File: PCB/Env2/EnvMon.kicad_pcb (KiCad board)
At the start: 2 copper layers, 70 x 70 mm, 37 parts, among them J1 LCD, J2 DC, J3 TEMP, J4 LCD, J5 Reset, J6 USB-C-Socket-H, J7 TC2030-USB-NL-DS, J8 T6793, U1 ESP32-S3-MINI-1, U2 SCD41, U3 MD8942, U7 SHT40, U8 VEML6040

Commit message: Tracked and SS
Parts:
- removed C5: 100nF, RevK:C_0402
- removed U7: SHT40, RevK:Sensirion_DFN-4_1.5x1.5mm_P0.5mm_SHT4x
- added C6: 100nF, RevK:C_0402, F.Cu at (107.8, 81.8)
- added R6: 10K, RevK:R_0402, F.Cu at (98.8, 92.0)
- added R7: 10K, RevK:R_0402, F.Cu at (98.8, 89.8)
- added U4: MCP9808_MSOP, Package_SO:MSOP-8_3x3mm_P0.65mm, F.Cu at (113.0, 78.2)
- J4: footprint RevK:PinSocket_1x08_P2.54mm_Vertical_SMD -> RevK:PinHeader_1x08_P2.54mm_Vertical; moved to B.Cu
- moved D19 7.50 mm to (90.0, 98.5)
- moved R3 5.85 mm to (114.5, 106.5)
- moved R4 4.00 mm to (114.5, 105.0)
- moved D20 2.61 mm to (102.8, 103.5), turned to 90 degrees
- moved C4 1.89 mm to (99.7, 97.1), turned to 90 degrees
- moved R13 1.52 mm to (121.0, 111.8), turned to 180 degrees
- moved C3 1.00 mm to (99.5, 82.0)
- moved R5 1.00 mm to (99.5, 83.0), turned to 180 degrees
- moved C1 0.50 mm to (80.5, 82.5), turned to 180 degrees
- moved C2 0.50 mm to (80.5, 83.5), turned to 180 degrees
- moved J4 0.50 mm to (126.5, 83.4), turned to 180 degrees
- moved J6 0.50 mm to (108.8, 104.0)
- moved U8 0.50 mm to (77.0, 76.5)
- moved J3 0.25 mm to (121.8, 119.0)
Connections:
- C4 pad 1: +3V3 -> +3.3V
- D19 pad 1: DC -> VDC
- D20 pad 1: DC -> VDC
- U1 pad 10: unconnected-(U1-GPIO6-Pad10) -> CS
- U1 pad 11: unconnected-(U1-GPIO7-Pad11) -> DC
- U1 pad 12: unconnected-(U1-GPIO8-Pad12) -> RST
- U1 pad 13: unconnected-(U1-GPIO9-Pad13) -> BL
- U1 pad 18: +3.3V -> unconnected-(U1-GPIO14-Pad18)
- U1 pad 32: unconnected-(U1-GPIO36-Pad32) -> LED
- U1 pad 41: LED -> unconnected-(U1-GPIO45-Pad41)
- U1 pad 8: unconnected-(U1-GPIO4-Pad8) -> DIN
- U1 pad 9: unconnected-(U1-GPIO5-Pad9) -> CLK
- U3 pad 5: DC -> VDC
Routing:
- net +3.3V: track 0.00 -> 230.6 mm, vias 0 -> 7
- net SDA: track 0.00 -> 132.3 mm, vias 0 -> 5
- net SCL: track 0.00 -> 126.5 mm, vias 0 -> 4
- net BL: track 0.00 -> 72.5 mm
- net TEMP: track 0.00 -> 70.4 mm, vias 0 -> 4
- net RST: track 0.00 -> 69.1 mm
- net DC: track 0.00 -> 67.2 mm
- net CLK: track 0.00 -> 64.8 mm
- net DIN: track 0.00 -> 64.4 mm
- net CS: track 0.00 -> 63.2 mm
- net D+: track 0.00 -> 42.7 mm, vias 0 -> 2
- net LED: track 0.00 -> 41.3 mm, vias 0 -> 2
- net D-: track 0.00 -> 36.1 mm, vias 0 -> 2
- net VDC: track 0.00 -> 22.5 mm, vias 0 -> 2
- net GND: track 0.00 -> 21.6 mm, vias 38 -> 98
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- added copper zone on F.Cu, net VBUS
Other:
- board text added: "${CURRENT_DATE}"
- board text added: "+"
- board text added: "12"
- board text added: "2.4{dblquote}LCD"
- board text added: "21"
- board text added: "2{dblquote}LCD"
- board text added: "36"
- board text added: "39 40"
- board text added: "4 5 6 7 8 9"
- board text added: "A"
- board text added: "AB"
- board text added: "DC"
- board text added: "DIN CLK CS DC RST BL"
- board text added: "DS18B20"
- board text added: "Environmental Monitor"
- board text added: "MCP9808"
- board text added: "SCD41"
- board text added: "SDA SCL"
- board text added: "T+H"
- board text added: "T6793 or"
- board text added: "TC2030"
- board text added: "VEML6040"

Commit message: Tracking
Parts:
- moved J5 0.21 mm to (90.0, 88.0)
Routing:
- net +3.3V: track 230.6 -> 231.6 mm
- added copper zone on F.Cu, net +3.3V
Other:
- board text added: "CO2 SENSOR"
- board text added: "Made in China for Andrews&Arnold Ltd"

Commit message: Render
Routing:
- net +3.3V: track 231.6 -> 231.0 mm

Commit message: Tweaks and render
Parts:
- added J10: Conn_01x01, RevK:PinHeader_1x01_P2.54mm_Vertical, F.Cu at (101.2, 120.8)
- added J11: Conn_01x01, RevK:PinHeader_1x01_P2.54mm_Vertical, F.Cu at (101.2, 123.8)
- added J12: Conn_01x01, RevK:PinHeader_1x01_P2.54mm_Vertical, F.Cu at (101.2, 114.5)
- added J9: Conn_01x01, RevK:PinHeader_1x01_P2.54mm_Vertical, F.Cu at (101.2, 111.5)
- J8: footprint Connector_PinSocket_2.54mm:PinSocket_1x06_P2.54mm_Vertical -> RevK:PinHeader_1x06_P2.54mm_Vertical
- moved J8 0.25 mm to (73.5, 111.0)
- moved V2 0.25 mm to (100.0, 125.2)
- moved J3 0.22 mm to (121.5, 119.1)
- turned U2 to 180 degrees
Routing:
- net SDA: track 132.1 -> 109.6 mm, vias 5 -> 6
- net SCL: track 126.1 -> 112.2 mm, vias 4 -> 3
- net GND: vias 98 -> 111
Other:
- board text added: "38 39"
- board text added: "External Temp Sensors"
- board text added: "SCL SDA"
- board text removed: "39 40"

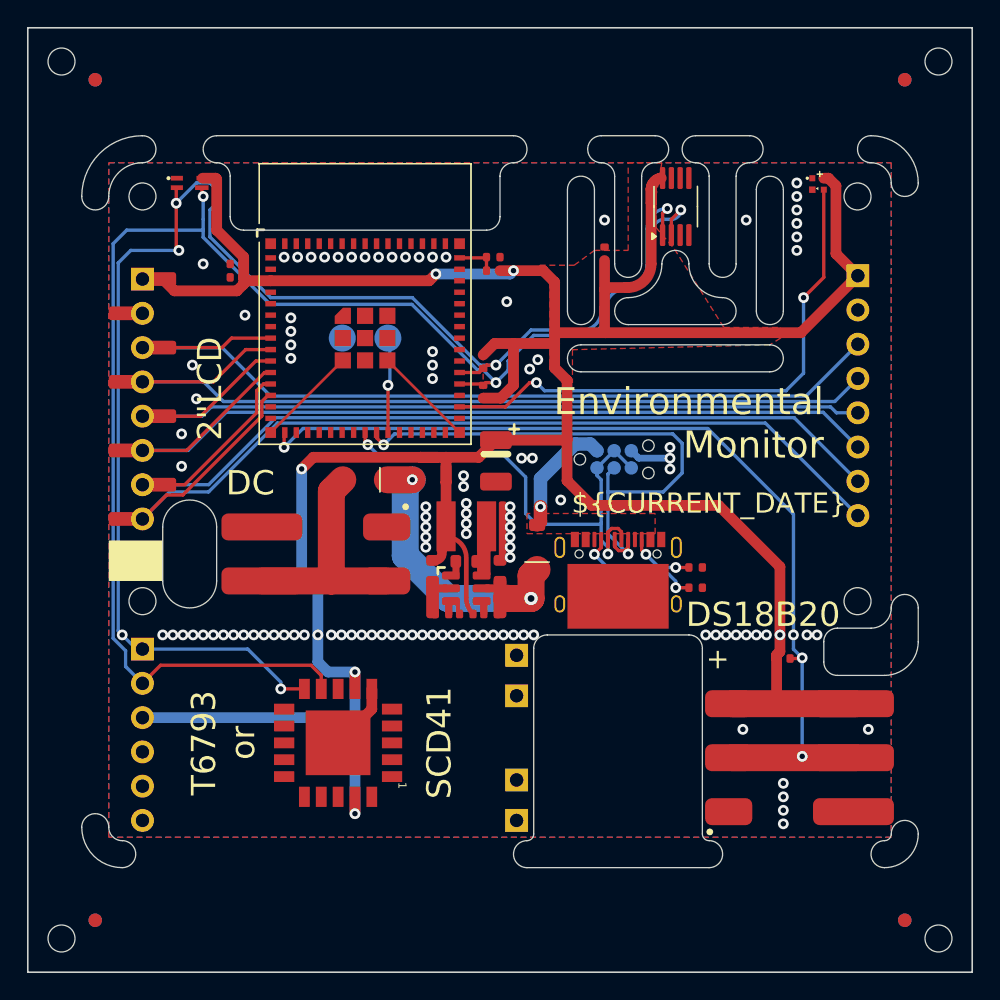
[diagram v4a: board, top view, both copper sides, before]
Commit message: Pressure sensor
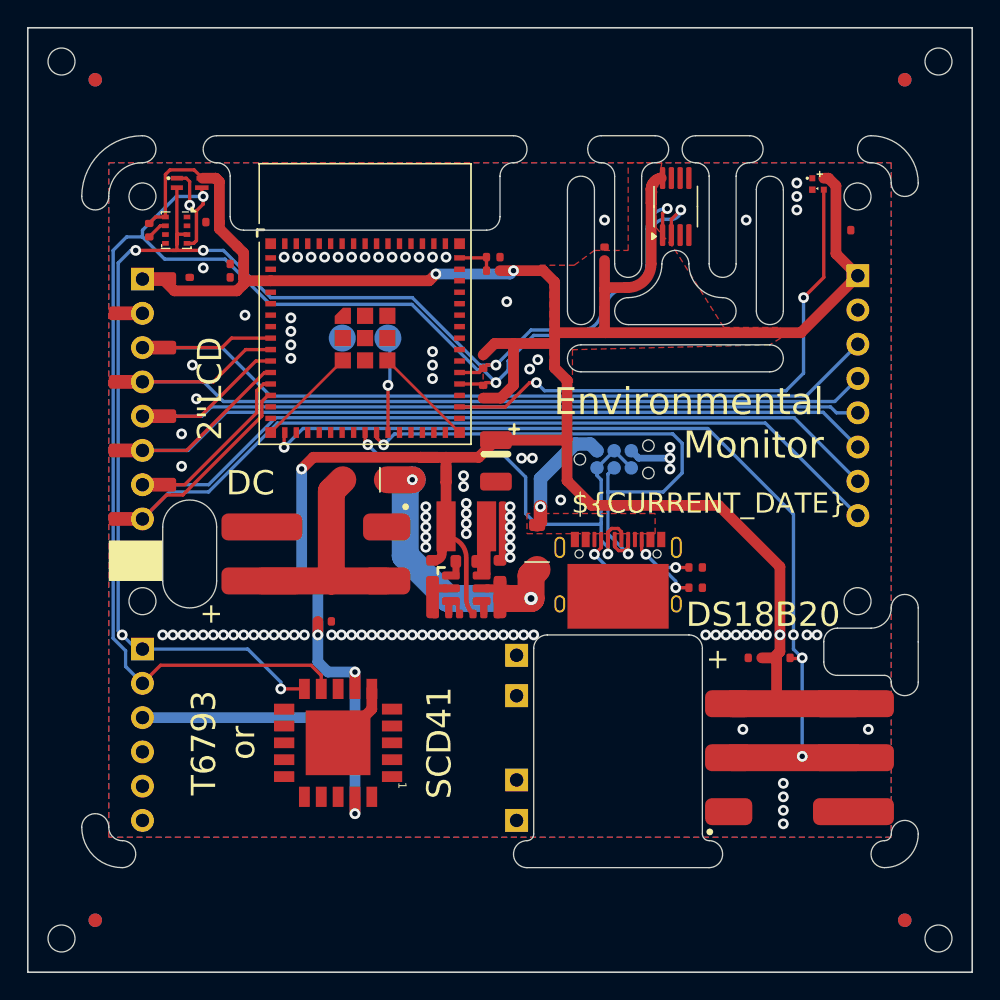
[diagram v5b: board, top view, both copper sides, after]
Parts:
- added C10: 100nF, RevK:C_0402, F.Cu at (78.7, 79.4)
- added C11: 100nF, RevK:C_0402, F.Cu at (118.9, 111.7)
- added C5: 100nF, RevK:C_0402, F.Cu at (87.0, 109.0)
- added C7: 100nF, RevK:C_0402, F.Cu at (77.0, 84.0)
- added C8: 100nF, RevK:C_0402, F.Cu at (125.5, 80.0)
- added C9: 100nF, RevK:C_0402, F.Cu at (74.0, 80.0)
- added U5: GZP6816D, Package_LGA:Bosch_LGA-8_2x2.5mm_P0.65mm_ClockwisePinNumbering, F.Cu at (76.0, 80.0)
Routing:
- net +3.3V: track 230.6 -> 240.5 mm
- net SCL: track 112.2 -> 119.0 mm
- net GND: track 21.6 -> 25.9 mm, vias 111 -> 109
- net SDA: track 109.6 -> 106.0 mm
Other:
- board text added: "GZP6816D"

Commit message: Silk screen
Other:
- board text added: "."

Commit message: SS
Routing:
- net D-: track 36.1 -> 36.6 mm
- net GND: vias 109 -> 118
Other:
- board text added: "-"

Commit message: New board
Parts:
- added C12: 100nF, RevK:C_0402, F.Cu at (103.0, 98.7)
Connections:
- J8 pad 3: +3.3V -> VBUS
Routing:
- net VBUS: track 9.00 -> 68.0 mm, vias 1 -> 3
- net +3.3V: track 240.5 -> 223.5 mm
- net GND: track 25.9 -> 29.8 mm, vias 118 -> 116
- net VDC: track 22.5 -> 24.0 mm
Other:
- board text added: "T6793 (USB 5V)"
- board text added: "or SCD41"
- board text removed: "SCD41"
- board text removed: "T6793 or"
